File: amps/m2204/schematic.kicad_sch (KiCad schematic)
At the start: 92 parts, among them J1 1/4 in, J2 1/4 in, J3 1/4 in, J4 1/4 in, J5 1/4 in, T1 1202-324, T2 789-139, T3 choke

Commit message: Fix: schematic sheets — real title block, fitted paper, no lettering through circuitry
Every sheet in the corpus shipped with an EMPTY title block ("Title:" and
"Date:" blank, default "Sheet /" furniture) laid onto a fixed A4/A3 page
regardless of the drawing's size, with prose annotations placed by hand
wherever a coordinate looked free when the amp was first drawn. The result
read as an unfinished alpha under a `verified` badge: KiCanvas's default view
is `zoom_to_page()`, so a 150 x 110 mm circuit on an A3 sheet opened as a
postage stamp, and later edits had pushed live circuitry under the prose.

schematic_lib.py — the builder now records each element as a (kind, points,
extra) tuple instead of a finished string, so `write()` can measure and move
what it emits:

- emits a real `(title_block …)` read from the amp's own meta.yaml — Title =
  designation + style, Date = the verification (or added) date, Rev = the
  verification status, Company = Circuit Codex, plus the licence and source
  URL as comments. Fixes all 34 sheets from one place;
- emits `(paper "User" w h)` cut to the drawing, translated to a fixed margin,
  with the bottom 34 mm strip reserved for the worksheet's title block. Sheet
  utilisation of the drawable area went from as low as ~20% to 92-98%;
- `note()` queues prose into a wrapped band under the circuit, and `caption()`
  places a section heading over the block it names, nudging it clear if it
  would print through anything;
- per-symbol default label offsets (the old single default printed every pot's
  value through its own wiper arrow and every transformer's designator through
  its body), plus `place_labels()`, which moves any designator/value block that
  would print over ink;
- transformers and chokes are drawn, not boxed: iron core between two windings,
  centre taps where the part has them, and an optional `spec` lettering slot for
  a ratio or impedance;
- `gnd()` takes a direction, because a flag defaulting to "down" at the HEAD of
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
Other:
- note added: "S2 is a two-pole standby switch: the drawing breaks both HT legs, and one pole is drawn here. T1 also carries the 6.3 V heater winding — black and orange leads with an earthed green centre tap — which is not drawn; nor is the mains indicator lamp the drawing shows across the primary, which carries no reference designator. See netlist.cir and meta.yaml."
- note removed: "Model 2204 — Master Volume lead 50-style · Circuit Codex · CC-BY-SA 4.0 · redrawn from circuit facts"
- note removed: "S2 is a two-pole standby switch: the drawing breaks both HT legs, and one pole is drawn here. T1 also carries the 6.3 V heater winding — black and orange leads with an earthed green centre tap — which is not drawn; nor is the"
- note removed: "mains indicator lamp the drawing shows across the primary, which carries no reference designator. See netlist.cir and meta.yaml."
- company: (none) -> Circuit Codex
- title: (none) -> M2204 — Master Volume lead 50-style

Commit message: Fix: rotated global labels lettered their net names outside the flag
Every global label this pipeline emitted carried (justify left) regardless of
rotation. KiCanvas — like KiCad — draws label text horizontally at 0/180 and
vertically at 90/270 and reads WHICH SIDE of the anchor it letters on from the
justification, so at 180 and 270 the name printed outside an empty flag
outline, struck through by the very wire it names: 219 labels at 180 deg
(including the input-jack flags at top-left of nearly every sheet, the first
glyphs a visitor reads) and 792 GND/rail flags at 270 whose names squeezed at
the flag mouth instead of lettering down the body. The library already
compensated rotation for property text (`pa`); this mirrors that logic for
global labels: justify right at 180/270, left at 0/90.

check_schematics gains the geometry clause whose absence let all 1011
instances through a "no lettering through circuitry" pass: it modelled the
flag box but never the label TEXT, so a name rendered on the wrong side was
invisible to it. The gate now proves justification compensates rotation on
every global label.

Two more things this exposed, fixed in the same engine pass:

- Placement now measures with the renderer's own Newstroke advance table
  (extracted from the vendored kicanvas.js) instead of a flat 0.68-em prose
  average that under-read part lettering by a quarter — the mechanism behind
  every "metered clean, printed through its neighbour" incident. The GATE
  deliberately keeps the coarse ruler: re-ruling it with renderer truth was
  tried and red-flagged 28 of 34 sheets over abutments three visual passes
  had already judged sub-visual (the two-rulers note in schematic_lib.py).
- place_captions' escape ladder runs further, because a banner caption
  measured truly is half again wider than the old estimate believed.

All 34 schematics regenerated; full gate suite green.

🤖 Generated with [Claude Code](https://claude.com/claude-code)

Co-Authored-By: Claude Fable 5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
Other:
- note added: "S2 is a two-pole standby switch: the drawing breaks both HT legs, and one pole is drawn here. T1 also carries the 6.3 V heater winding — black and orange leads with an earthed green centre tap — which is not drawn; nor is the mains indicator lamp the drawing shows across the primary, which carries no reference"
- note added: "designator. See netlist.cir and meta.yaml."
- note removed: "S2 is a two-pole standby switch: the drawing breaks both HT legs, and one pole is drawn here. T1 also carries the 6.3 V heater winding — black and orange leads with an earthed green centre tap — which is not drawn; nor is the mains indicator lamp the drawing shows across the primary, which carries no reference designator. See netlist.cir and meta.yaml."

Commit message: Fix: deterministic schematic ids and wires split at every join
- _u() is uuid5 over (amp id, emission order), so a regeneration of an
  unchanged script is byte-identical and a drift gate becomes possible
- write() splits wire segments at symbol pins, wire ends and junction dots,
  so the file connects exactly what the drawing shows under KiCad's
  endpoint-only semantics (270 pins were on a wire's interior; net
  partitions unchanged on all 38 sheets)
- all sheets regenerated; aa864-bassman title block was stale (draft) and
  now matches meta.yaml (verified)

Co-Authored-By: Claude Fable 5.1 <noreply@anthropic.com>
Claude-Session: https://claude.ai/code/session_01KBMfdh37HmCL2iWcBiL5J1
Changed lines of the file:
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@@
   (wire (pts (xy 62.1 168.11) (xy 70.1 168.11))
     (stroke (width 0) (type default)))
-  (wire (pts (xy 70.1 132.11) (xy 70.1 168.11))
+  (wire (pts (xy 70.1 132.11) (xy 70.1 150.11))
+    (stroke (width 0) (type default)))
+  (wire (pts (xy 70.1 150.11) (xy 70.1 168.11))
     (stroke (width 0) (type default)))
   (junction (at 70.1 150.11) (diameter 0) (color 0 0 0 0))
@@
   (wire (pts (xy 48.1 195.92) (xy 48.1 196.11))
     (stroke (width 0) (type default)))
-  (wire (pts (xy 22.1 196.11) (xy 86.29 196.11))
+  (wire (pts (xy 22.1 196.11) (xy 34.1 196.11))
+    (stroke (width 0) (type default)))
+  (wire (pts (xy 34.1 196.11) (xy 42.1 196.11))
+    (stroke (width 0) (type default)))
+  (wire (pts (xy 42.1 196.11) (xy 48.1 196.11))
+    (stroke (width 0) (type default)))
+  (wire (pts (xy 48.1 196.11) (xy 86.29 196.11))
     (stroke (width 0) (type default)))
   (junction (at 42.1 196.11) (diameter 0) (color 0 0 0 0))
@@
   (wire (pts (xy 157.18 229.03) (xy 166.1 229.03))
     (stroke (width 0) (type default)))
-  (wire (pts (xy 110.99 239.19) (xy 135.02 239.19))
+  (wire (pts (xy 110.99 239.19) (xy 128.1 239.19))
+    (stroke (width 0) (type default)))
+  (wire (pts (xy 128.1 239.19) (xy 135.02 239.19))
     (stroke (width 0) (type default)))
   (symbol (lib_id "cx:DIODE_SS") (at 140.1 239.19 0) (unit 1)
@@
   (wire (pts (xy 157.18 239.19) (xy 166.1 239.19))
     (stroke (width 0) (type default)))
-  (wire (pts (xy 166.1 229.03) (xy 166.1 239.19))
+  (wire (pts (xy 166.1 229.03) (xy 166.1 234.11))
+    (stroke (width 0) (type default)))
+  (wire (pts (xy 166.1 234.11) (xy 166.1 239.19))
     (stroke (width 0) (type default)))
   (wire (pts (xy 166.1 234.11) (xy 171.56 234.11))
@@
   (wire (pts (xy 206.1 234.11) (xy 208.48 234.11))
     (stroke (width 0) (type default)))
-  (wire (pts (xy 223.72 234.11) (xy 239.56 234.11))
+  (wire (pts (xy 223.72 234.11) (xy 232.1 234.11))
+    (stroke (width 0) (type default)))
+  (wire (pts (xy 232.1 234.11) (xy 239.56 234.11))
     (stroke (width 0) (type default)))
   (junction (at 232.1 234.11) (diameter 0) (color 0 0 0 0))
@@
   (wire (pts (xy 164.1 256.11) (xy 170.29 256.11))
     (stroke (width 0) (type default)))
-  (wire (pts (xy 177.91 256.11) (xy 188.1 256.11))
+  (wire (pts (xy 177.91 256.11) (xy 182.1 256.11))
+    (stroke (width 0) (type default)))
+  (wire (pts (xy 182.1 256.11) (xy 188.1 256.11))
     (stroke (width 0) (type default)))
   (junction (at 182.1 256.11) (diameter 0) (color 0 0 0 0))

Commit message: Add: real tube pin numbers and readable valve glyphs on every schematic
Phase B of the drawing program. A factory service sheet numbers every tube
pin, because the number is what a technician puts a probe on. This corpus
printed none, and the numbers hidden in its symbols were positional
placeholders (P=1, G=2, K=3) that would have published a 6V6GT's plate as
pin 1 when it is pin 3.

1055 electrodes now carry the real number, 1027 lettered (27 are shared
filaments deduped, 1 dropped for want of clear space on the 6G2). Resolved per
instance from reference/tubes/<slug>.yaml through the same alias resolution the
layout renderer uses, so a 12AX7 section and a 6SL7 section each get their own
basing. A valve whose basing the corpus does not carry prints nothing rather
than a wrong number.

Section letters and basing units are now separate things, which cost a detour
worth recording. The RCA 12AX7-A sheet reads "Pin 1 - Plate of Unit No.2 ...
Pin 6 - Plate of Unit No.1", so unit numbering is not pin order; the 5Y3 and
GZ34 number their units in opposite pin order, so nothing positional can
express it. But the section LETTER is a designator, not a basing fact: this
corpus, like every technician, calls the first stage in signal order V1A, and
five amps' prose already did. On four amps the factory sheets put that first
stage on the other half -- the AA764's own schematic prints +200 V on pin 1 --
so those drawings now state their unit explicitly, each citing its source, and
no letter, netlist, parts list or layout comment changed. 183 layout comments
agree with the printed numbers, 0 disagree. A guard fires if two halves of one
bottle resolve to the same unit, which is exactly how this was found.

Glyphs: the cathode gains a bracket and filament hairpin so it can no longer be
confused with the plate bar, the pentode's screen sits on its own row, and a
rectifier draws as one envelope over its sections instead of two apparent
bottles. Line weights are scaled per sheet to a co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
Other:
- note added: "1"
- note added: "2"
- note added: "3"
- note added: "4"
- note added: "5"
- note added: "6"
- note added: "7"
- note added: "8"

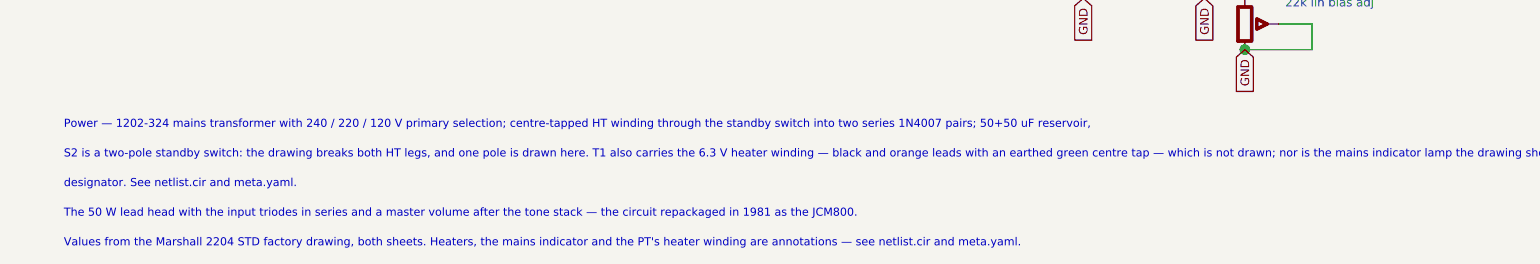
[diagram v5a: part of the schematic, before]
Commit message: Fix: schematic sheet notes no longer name repository files
Thirty-seven committed sheets rendered footnotes and section notes such as
"Heaters and PT primary omitted — see netlist.cir and meta.yaml" or
"excluded from netlist.cir (notes.md)" to visitors through KiCanvas. The
prose sweeps never counted sheets. Rewritten in the site's own words — the
netlist, the sources list, the circuit story, the parts list, the board
drawing — in 59 strings across 33 draw scripts, keeping every technical
claim as it was; the three tone sheets (6G4, 6G5, 6G6-B) are under repair
elsewhere and keep theirs for now. The sweep touched only strings passed to
the sheet's note, text, caption and footnote calls, never a path or a value.

Gates: check_schematics 40/0, connectivity 0 isolated pins;
verify_schematic_nets 40 clean; only the regenerated sheets and their served
copies changed.

Co-Authored-By: Claude Fable 5.1 <noreply@anthropic.com>
Claude-Session: https://claude.ai/code/session_01KBMfdh37HmCL2iWcBiL5J1
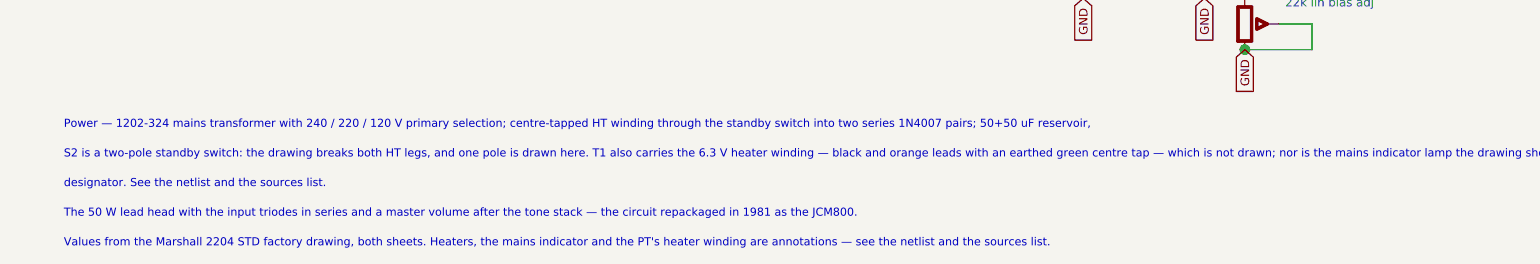
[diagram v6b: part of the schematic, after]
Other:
- note added: "Values from the Marshall 2204 STD factory drawing, both sheets. Heaters, the mains indicator and the PT's heater winding are annotations — see the netlist and the sources list."
- note added: "designator. See the netlist and the sources list."
- note removed: "Values from the Marshall 2204 STD factory drawing, both sheets. Heaters, the mains indicator and the PT's heater winding are annotations — see netlist.cir and meta.yaml."
- note removed: "designator. See netlist.cir and meta.yaml."
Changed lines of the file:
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@@
   (text "S2 is a two-pole standby switch: the drawing breaks both HT legs, and one pole is drawn here. T1 also carries the 6.3 V heater winding — black and orange leads with an earthed green centre tap — which is not drawn; nor is the mains indicator lamp the drawing shows across the primary, which carries no reference" (at 12.7 286.908 0)
     (effects (font (size 1.2 1.2)) (justify left)))
-  (text "designator. See netlist.cir and meta.yaml." (at 12.7 291.308 0)
+  (text "designator. See the netlist and the sources list." (at 12.7 291.308 0)
     (effects (font (size 1.2 1.2)) (justify left)))
   (text "The 50 W lead head with the input triodes in series and a master volume after the tone stack — the circuit repackaged in 1981 as the JCM800." (at 12.7 295.708 0)
     (effects (font (size 1.2 1.2)) (justify left)))
-  (text "Values from the Marshall 2204 STD factory drawing, both sheets. Heaters, the mains indicator and the PT's heater winding are annotations — see netlist.cir and meta.yaml." (at 12.7 300.108 0)
+  (text "Values from the Marshall 2204 STD factory drawing, both sheets. Heaters, the mains indicator and the PT's heater winding are annotations — see the netlist and the sources list." (at 12.7 300.108 0)
     (effects (font (size 1.2 1.2)) (justify left)))
   (sheet_instances (path "/" (page "1")))
